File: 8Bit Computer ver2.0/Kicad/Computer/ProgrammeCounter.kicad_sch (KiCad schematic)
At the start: 16 parts, among them IC182 SN74F521DWR, IC183 SN74F521DWR, IC184 SN74LVC1G14DBVR, IC185 SN74LVC1G14DBVR, IC65 SN74HCS4075DR, IC66 SN74LVC1G32DBVR, IC67 SN74LVC1G32DBVR, IC68 SN74LVC1G08DBVR, IC69 CY74FCT163CTSOC, IC70 CY74FCT163CTSOC, IC71 CY74FCT163CTSOC, IC72 CY74FCT163CTSOC, IC73 SN74LVC1G14DBVR, IC74 SN74LVC1G14DBVR

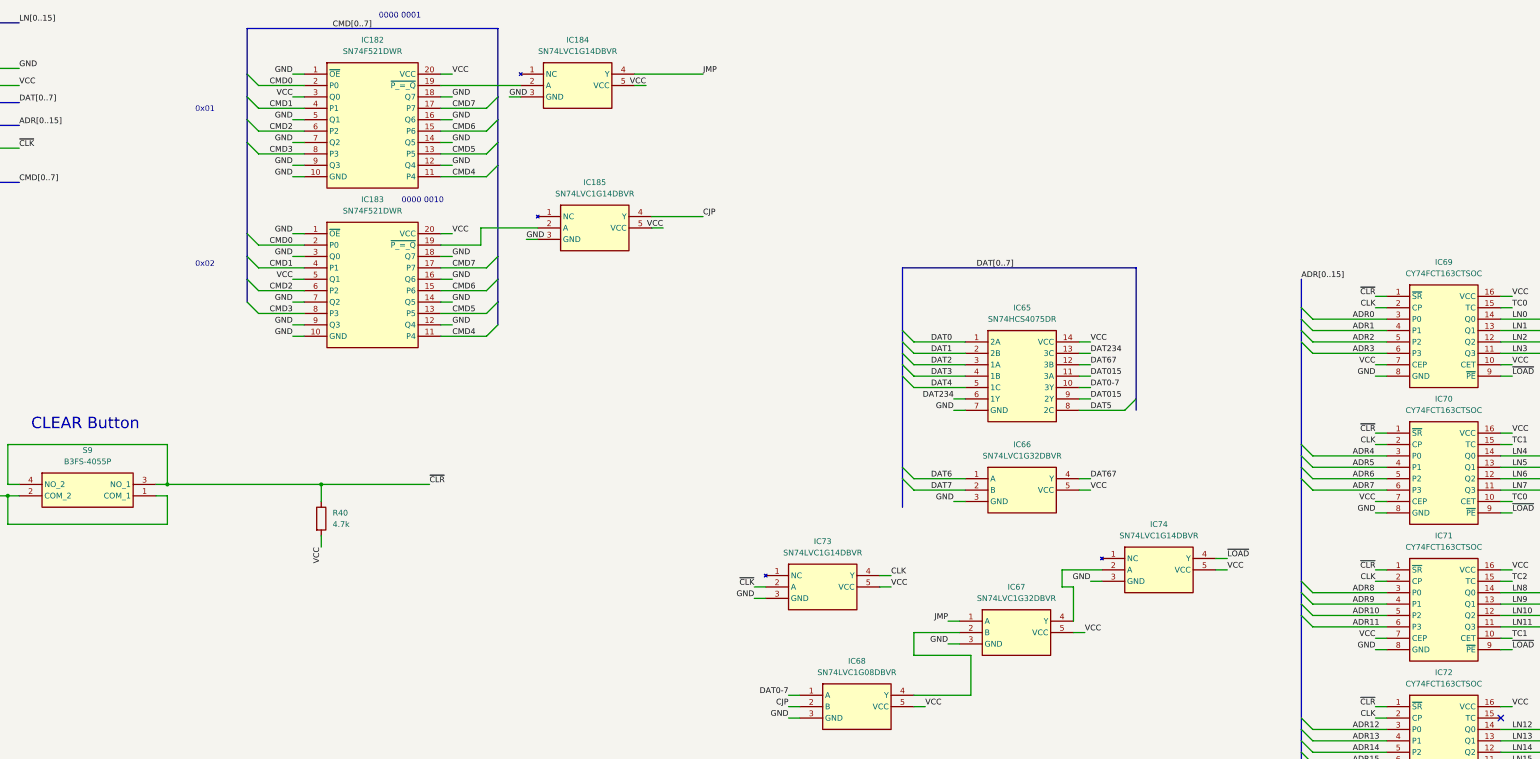
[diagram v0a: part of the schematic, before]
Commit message: Kicad SCH/PCB
Kicad SCH/PCB:
changed the References in SCH
began with INOUTPUT module nearly done
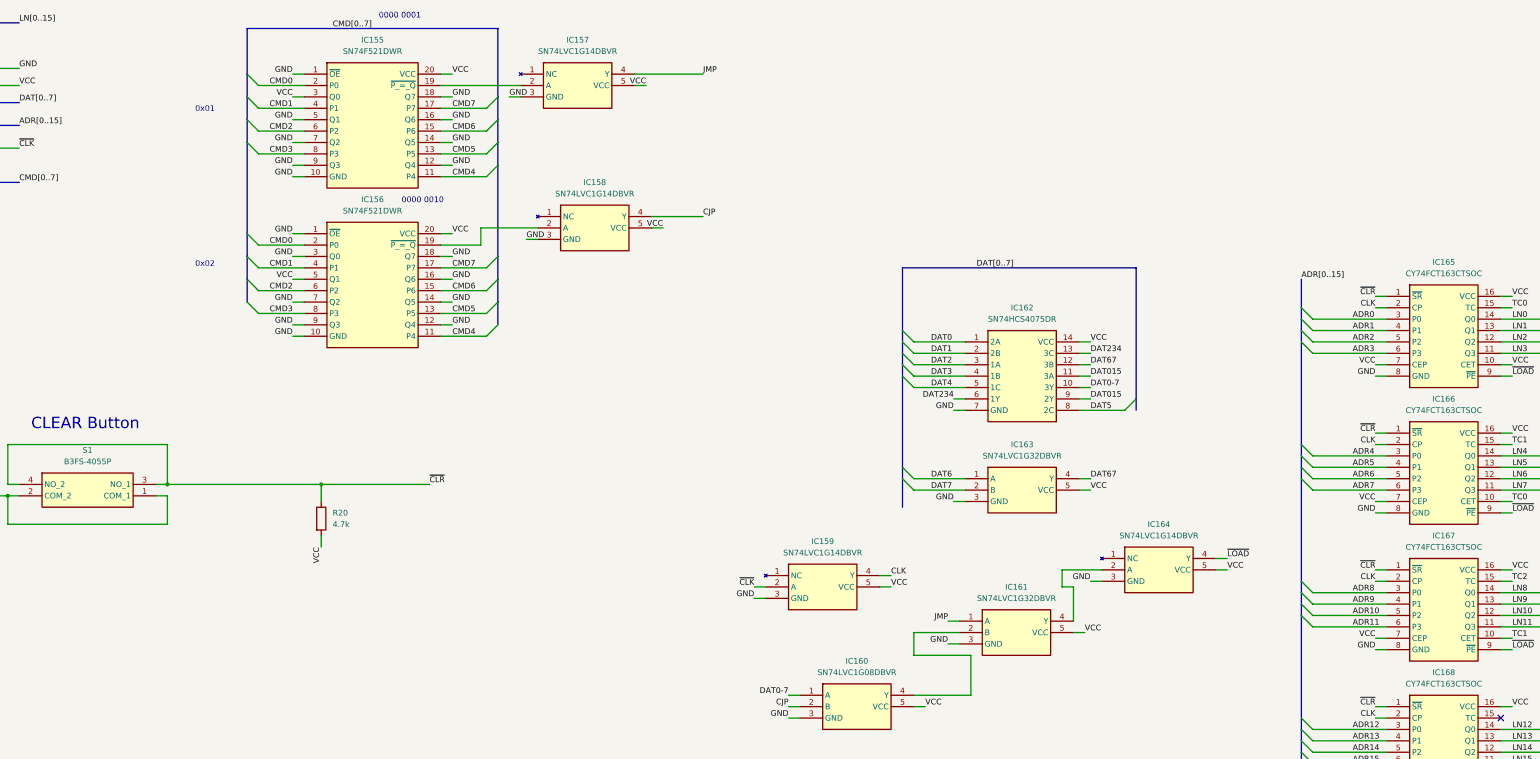
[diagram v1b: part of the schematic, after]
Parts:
- renumbered IC182 to IC155, IC183 to IC156, IC184 to IC157, IC185 to IC158, IC73 to IC159, IC68 to IC160, IC67 to IC161, IC65 to IC162, IC66 to IC163, IC74 to IC164, IC69 to IC165, IC70 to IC166, IC71 to IC167, IC72 to IC168, R40 to R20, S9 to S1
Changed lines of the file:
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@@
 		(dnp no)
 		(fields_autoplaced yes)
-		(property "Reference" "IC72"
+		(property "Reference" "IC168"
 			(at 356.87 209.55 0)
 			(effects
@@
 			(project "Computer"
 				(path "/1196a00e-6878-4d6d-82b7-9e052dfe7c14/94b0c6d4-a0ed-4382-b2de-ee1cd48dbaa6"
-					(reference "IC72")
+					(reference "IC168")
 					(unit 1)
 				)
@@
 		(dnp no)
 		(fields_autoplaced yes)
-		(property "Reference" "IC74"
+		(property "Reference" "IC164"
 			(at 293.37 176.53 0)
 			(effects
@@
 			(project ""
 				(path "/1196a00e-6878-4d6d-82b7-9e052dfe7c14/94b0c6d4-a0ed-4382-b2de-ee1cd48dbaa6"
-					(reference "IC74")
+					(reference "IC164")
 					(unit 1)
 				)
@@
 		(dnp no)
 		(fields_autoplaced yes)
-		(property "Reference" "IC185"
+		(property "Reference" "IC158"
 			(at 167.64 100.33 0)
 			(effects
@@
 			(project "Computer"
 				(path "/1196a00e-6878-4d6d-82b7-9e052dfe7c14/94b0c6d4-a0ed-4382-b2de-ee1cd48dbaa6"
-					(reference "IC185")
+					(reference "IC158")
 					(unit 1)
 				)
@@
 		(dnp no)
 		(fields_autoplaced yes)
-		(property "Reference" "IC70"
+		(property "Reference" "IC166"
 			(at 356.87 148.59 0)
 			(effects
@@
 			(project "Computer"
 				(path "/1196a00e-6878-4d6d-82b7-9e052dfe7c14/94b0c6d4-a0ed-4382-b2de-ee1cd48dbaa6"
-					(reference "IC70")
+					(reference "IC166")
 					(unit 1)
 				)
@@
 		(dnp no)
 		(fields_autoplaced yes)
-		(property "Reference" "S9"
+		(property "Reference" "S1"
 			(at 54.61 160.02 0)
 			(effects
@@
 			(project "Computer"
 				(path "/1196a00e-6878-4d6d-82b7-9e052dfe7c14/94b0c6d4-a0ed-4382-b2de-ee1cd48dbaa6"
-					(reference "S9")
+					(reference "S1")
 					(unit 1)
 				)
@@
 		(dnp no)
 		(fields_autoplaced yes)
-		(property "Reference" "IC71"
+		(property "Reference" "IC167"
 			(at 356.87 179.07 0)
 			(effects
@@
 			(project "Computer"
 				(path "/1196a00e-6878-4d6d-82b7-9e052dfe7c14/94b0c6d4-a0ed-4382-b2de-ee1cd48dbaa6"
-					(reference "IC71")
+					(reference "IC167")
 					(unit 1)
 				)
@@
 		(dnp no)
 		(fields_autoplaced yes)
-		(property "Reference" "IC182"
+		(property "Reference" "IC155"
 			(at 118.11 68.58 0)
 			(effects
@@
 			(project "Computer"
 				(path "/1196a00e-6878-4d6d-82b7-9e052dfe7c14/94b0c6d4-a0ed-4382-b2de-ee1cd48dbaa6"
-					(reference "IC182")
+					(reference "IC155")
 					(unit 1)
 				)
@@
 		(dnp no)
 		(fields_autoplaced yes)
-		(property "Reference" "IC184"
+		(property "Reference" "IC157"
 			(at 163.83 68.58 0)
 			(effects
@@
 			(project "Computer"
 				(path "/1196a00e-6878-4d6d-82b7-9e052dfe7c14/94b0c6d4-a0ed-4382-b2de-ee1cd48dbaa6"
-					(reference "IC184")
+					(reference "IC157")
 					(unit 1)
 				)
@@
 		(dnp no)
 		(fields_autoplaced yes)
-		(property "Reference" "IC67"
+		(property "Reference" "IC161"
 			(at 261.62 190.5 0)
 			(effects
@@
 			(project ""
 				(path "/1196a00e-6878-4d6d-82b7-9e052dfe7c14/94b0c6d4-a0ed-4382-b2de-ee1cd48dbaa6"
-					(reference "IC67")
+					(reference "IC161")
 					(unit 1)
 				)
@@
 		(dnp no)
 		(fields_autoplaced yes)
-		(property "Reference" "IC65"
+		(property "Reference" "IC162"
 			(at 262.89 128.27 0)
 			(effects
@@
 			(project ""
 				(path "/1196a00e-6878-4d6d-82b7-9e052dfe7c14/94b0c6d4-a0ed-4382-b2de-ee1cd48dbaa6"
-					(reference "IC65")
+					(reference "IC162")
 					(unit 1)
 				)
@@
 		(dnp no)
 		(fields_autoplaced yes)
-		(property "Reference" "IC68"
+		(property "Reference" "IC160"
 			(at 226.06 207.01 0)
 			(effects
@@
 			(project ""
 				(path "/1196a00e-6878-4d6d-82b7-9e052dfe7c14/94b0c6d4-a0ed-4382-b2de-ee1cd48dbaa6"
-					(reference "IC68")
+					(reference "IC160")
 					(unit 1)
 				)
@@
 		(dnp no)
 		(fields_autoplaced yes)
-		(property "Reference" "IC183"
+		(property "Reference" "IC156"
 			(at 118.11 104.14 0)
 			(effects
@@
 			(project "Computer"
 				(path "/1196a00e-6878-4d6d-82b7-9e052dfe7c14/94b0c6d4-a0ed-4382-b2de-ee1cd48dbaa6"
-					(reference "IC183")
+					(reference "IC156")
 					(unit 1)
 				)
@@
 		(dnp no)
 		(fields_autoplaced yes)
-		(property "Reference" "IC73"
+		(property "Reference" "IC159"
 			(at 218.44 180.34 0)
 			(effects
@@
 			(project ""
 				(path "/1196a00e-6878-4d6d-82b7-9e052dfe7c14/94b0c6d4-a0ed-4382-b2de-ee1cd48dbaa6"
-					(reference "IC73")
+					(reference "IC159")
 					(unit 1)
 				)
@@
 		(dnp no)
 		(fields_autoplaced yes)
-		(property "Reference" "R40"
+		(property "Reference" "R20"
 			(at 109.22 173.9899 0)
 			(effects
@@
 			(project "Computer"
 				(path "/1196a00e-6878-4d6d-82b7-9e052dfe7c14/94b0c6d4-a0ed-4382-b2de-ee1cd48dbaa6"
-					(reference "R40")
+					(reference "R20")
 					(unit 1)
 				)
@@
 		(dnp no)
 		(fields_autoplaced yes)
-		(property "Reference" "IC69"
+		(property "Reference" "IC165"
 			(at 356.87 118.11 0)
 			(effects
@@
 			(project ""
 				(path "/1196a00e-6878-4d6d-82b7-9e052dfe7c14/94b0c6d4-a0ed-4382-b2de-ee1cd48dbaa6"
-					(reference "IC69")
+					(reference "IC165")
 					(unit 1)
 				)
@@
 		(dnp no)
 		(fields_autoplaced yes)
-		(property "Reference" "IC66"
+		(property "Reference" "IC163"
 			(at 262.89 158.75 0)
 			(effects
@@
 			(project ""
 				(path "/1196a00e-6878-4d6d-82b7-9e052dfe7c14/94b0c6d4-a0ed-4382-b2de-ee1cd48dbaa6"
-					(reference "IC66")
+					(reference "IC163")
 					(unit 1)
 				)

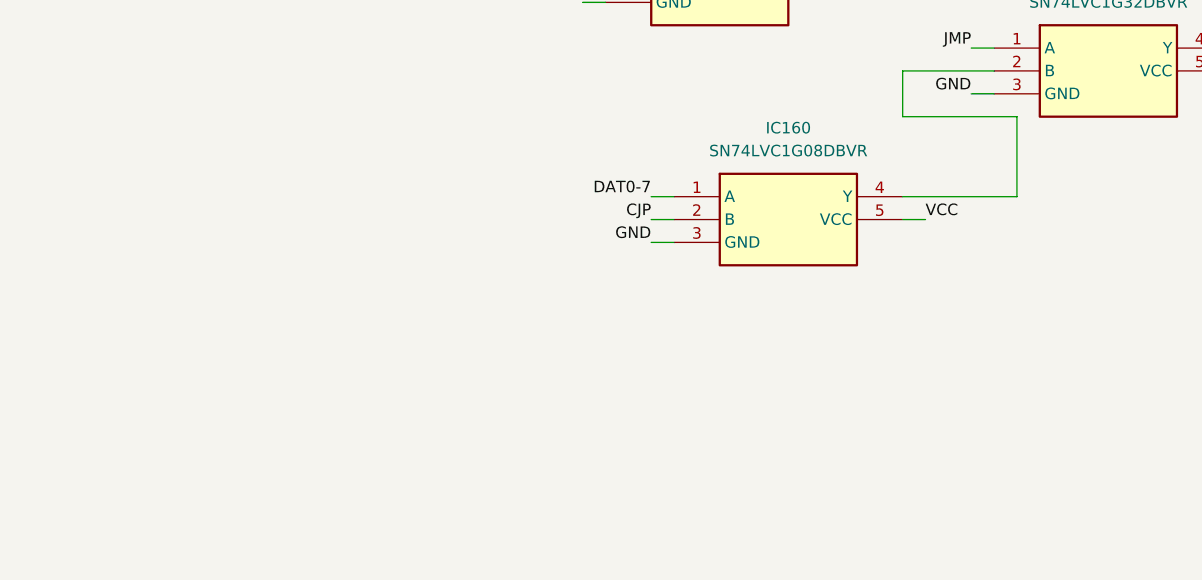
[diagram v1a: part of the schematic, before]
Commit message: Kicad,parts
parts:
added 1N4148 Diode SMD
Kicad:
fixed some routings of Schematic
created Flash mem and RAM PCB
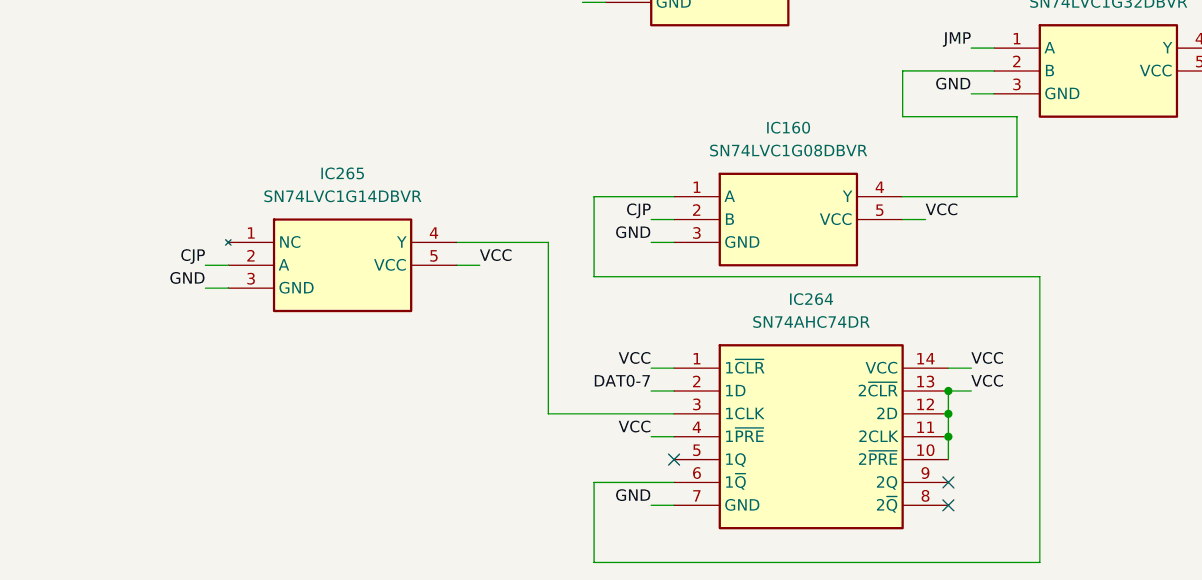
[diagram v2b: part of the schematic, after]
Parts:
- added IC264: SN74AHC74DR, Samacsys:SOIC127P600X175-14N, symbol Samacsys:SN74AHC74DR
- added IC265: SN74LVC1G14DBVR, Samacsys:SOT95P280X145-5N, symbol Samacsys:SN74LVC1G14DBVR
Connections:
- net CJP: now also IC265.2 (A)
- net DAT0-7: now also IC264.2 (1D); no longer IC160.1 (A)
- net GND: now also IC264.7 (GND), IC265.3 (GND)
- net VCC: now also IC264.1 (1~{CLR}), IC264.10 (2~{PRE}), IC264.11 (2CLK), IC264.12 (2D), IC264.13 (2~{CLR}), IC264.14 (VCC), IC264.4 (1~{PRE}), IC265.5 (VCC)
- new net: IC264.3 (1CLK), IC265.4 (Y)
- new net: IC160.1 (A), IC264.6 (1~{Q})
- no-connect marks 1 -> 4

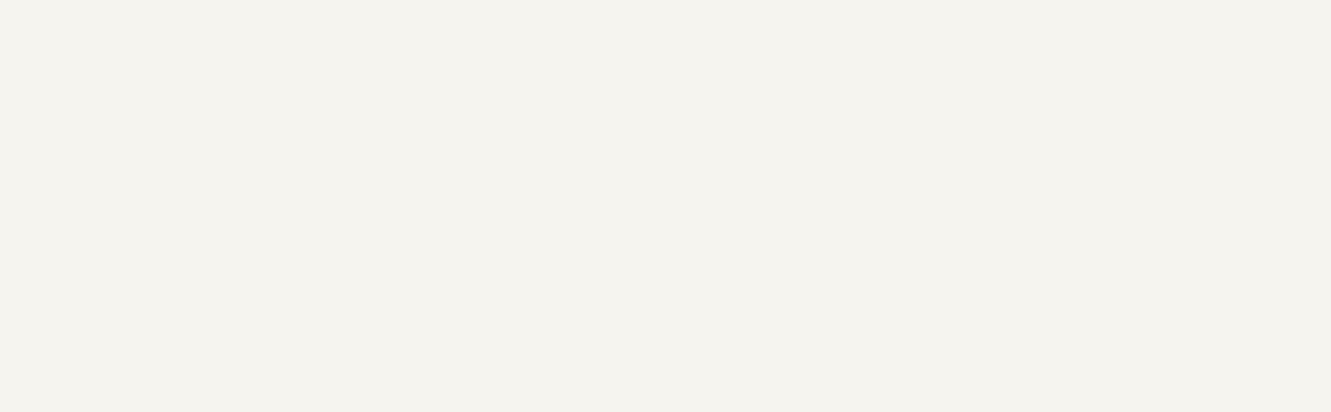
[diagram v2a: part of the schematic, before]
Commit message: Kicad
added the Programme Counter und Dat to adr module
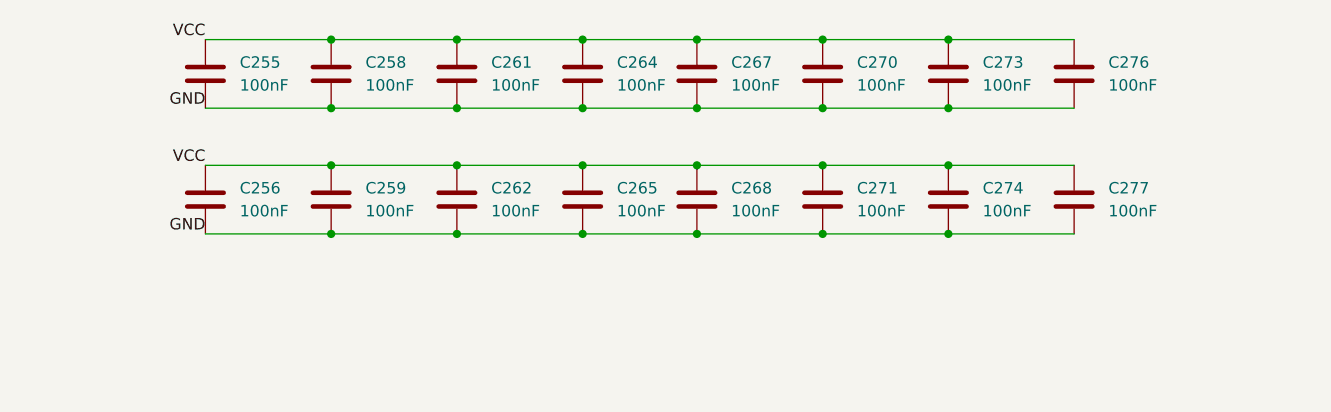
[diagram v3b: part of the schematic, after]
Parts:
- added C255, C256, C258, C259, C261, C262, C264, C265, C267, C268, C270, C271, C273, C274, C276, C277: 100nF, Capacitor_SMD:C_1206_3216Metric_Pad1.33x1.80mm_HandSolder, symbol Device:C
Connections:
- net GND: now also C255.1, C256.1, C258.1, C259.1, C261.1, C262.1, C264.1, C265.1, C267.1, C268.1, C270.1, C271.1, C273.1, C274.1, C276.1, C277.1
- net VCC: now also C255.2, C256.2, C258.2, C259.2, C261.2, C262.2, C264.2, C265.2, C267.2, C268.2, C270.2, C271.2, C273.2, C274.2, C276.2, C277.2

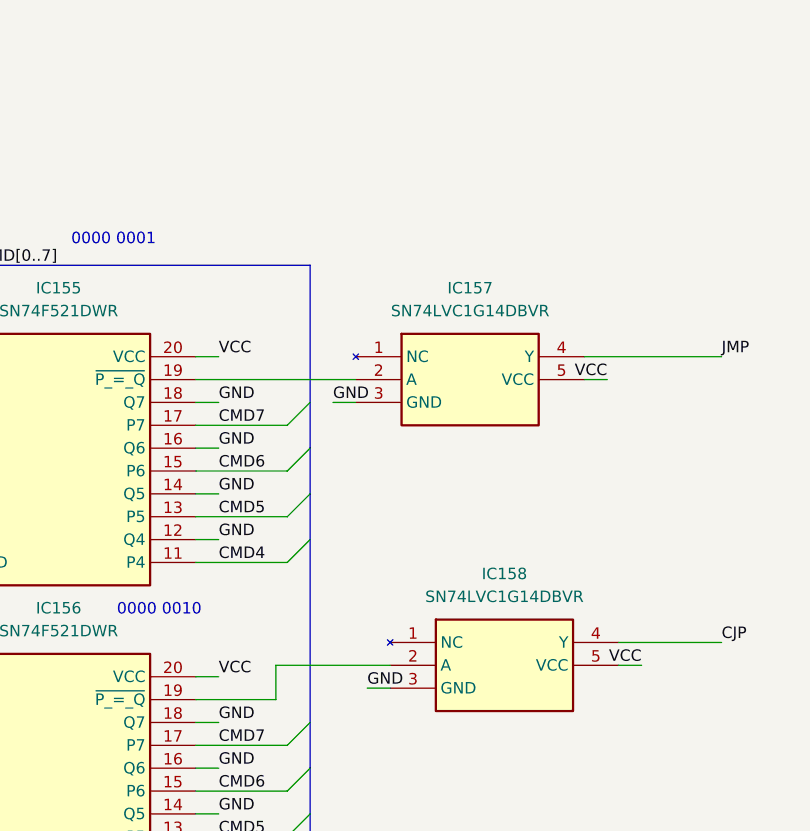
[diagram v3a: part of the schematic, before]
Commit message: Kicad
added 10pin 2,54mm Header
finished ALU PCB and added pin Header for extra use (DAT,ADR,CMD,Ddis,CLK)
31.12-06.01 about +60hr for ALU
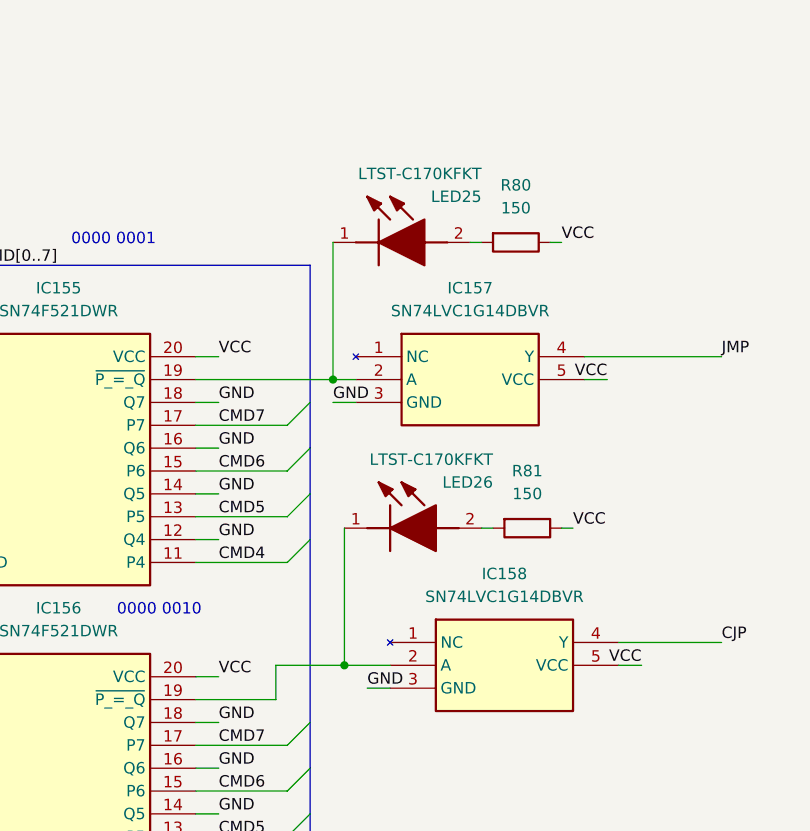
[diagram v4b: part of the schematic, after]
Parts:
- added LED25, LED26: LTST-C170KFKT, Samacsys:LEDC2012X120N, symbol Samacsys:LTST-C170KFKT
- added R80, R81: 150, Resistor_SMD:R_1206_3216Metric_Pad1.30x1.75mm_HandSolder, symbol Device:R
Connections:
- net VCC: now also R80.1, R81.1
- net at IC156.19 (~{P_=_Q}), IC158.2 (A): now also LED26.1 (K)
- net at IC155.19 (~{P_=_Q}), IC157.2 (A): now also LED25.1 (K)
- new net: LED26.2 (A), R81.2
- new net: LED25.2 (A), R80.2
